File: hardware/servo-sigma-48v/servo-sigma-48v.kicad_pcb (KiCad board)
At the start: 4 copper layers, 71.7 x 73.2 mm, 198 parts, among them J1 CONN_01X02, J10 Conn_01x03, J11 Conn_01x03, J2 CONN_02X05, J3 CONN_01X03, J4 Conn_01x03, J5 Conn_01x05, J6 629_105_150_921, J7 CONN_01X02, J8 Conn_01x03, J9 Conn_01x03, Q1 STL160NS3LLH7, Q2 STL160NS3LLH7, Q3 STL160NS3LLH7, Q4 STL160NS3LLH7, Q5 STL160NS3LLH7, Q6 STL160NS3LLH7, Q7 STL160NS3LLH7, Q8 STL160NS3LLH7, SW1 SW_DIP_x08, SW2 SW_DIP_x08, U1 ST1S14, U10 OPA4374, U11 L6398, U12 SN65HVD75DGKR, U2 TPS70950, U3 SN65HVD75DGKR, U4 L6398, U5 STM32F411RETx, U6 L6398, U7 L6398, U8 TPS70933, U9 OPA4374, Y1 ABM3-8.000MHZ-D2Y-T

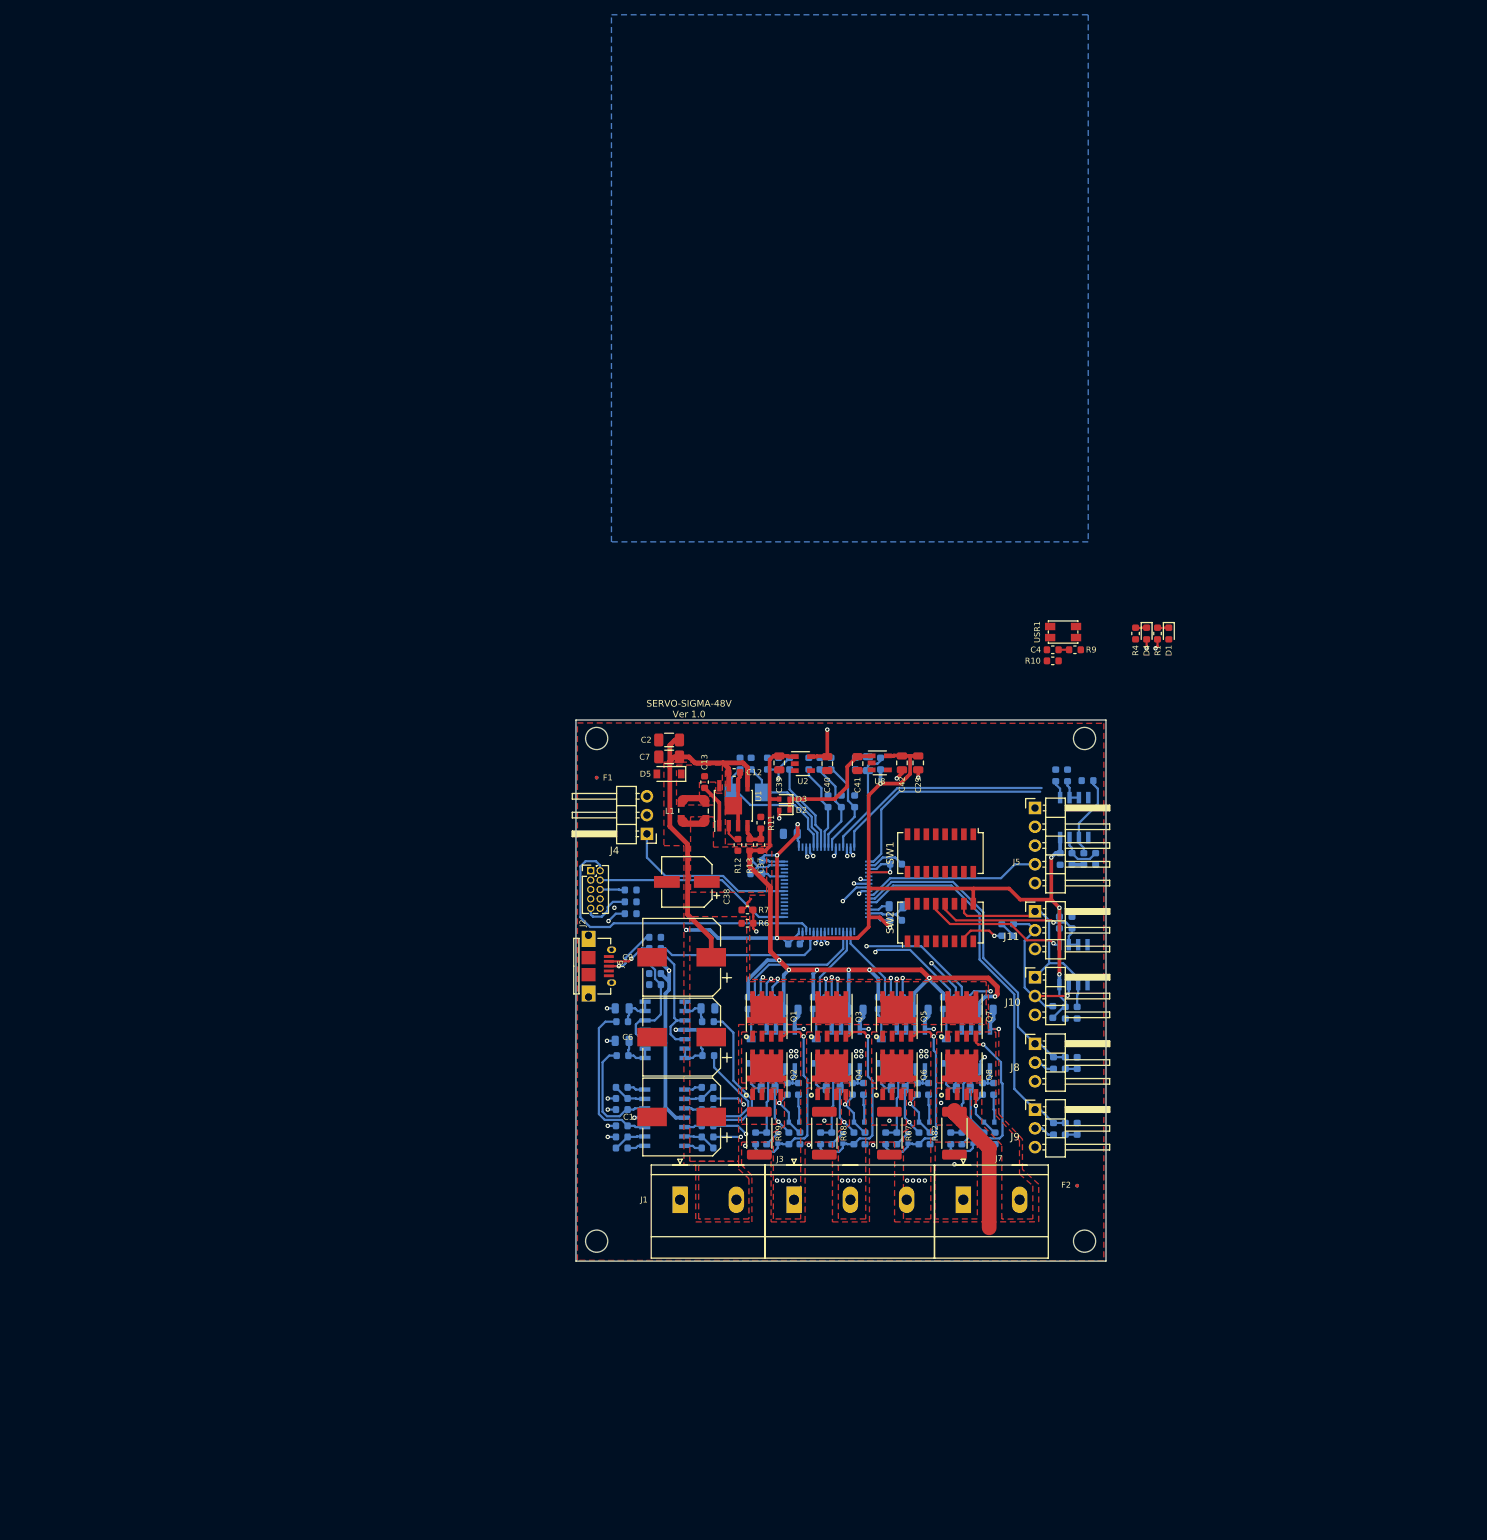
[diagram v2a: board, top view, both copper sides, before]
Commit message: Changed the MCU to use 100 pin
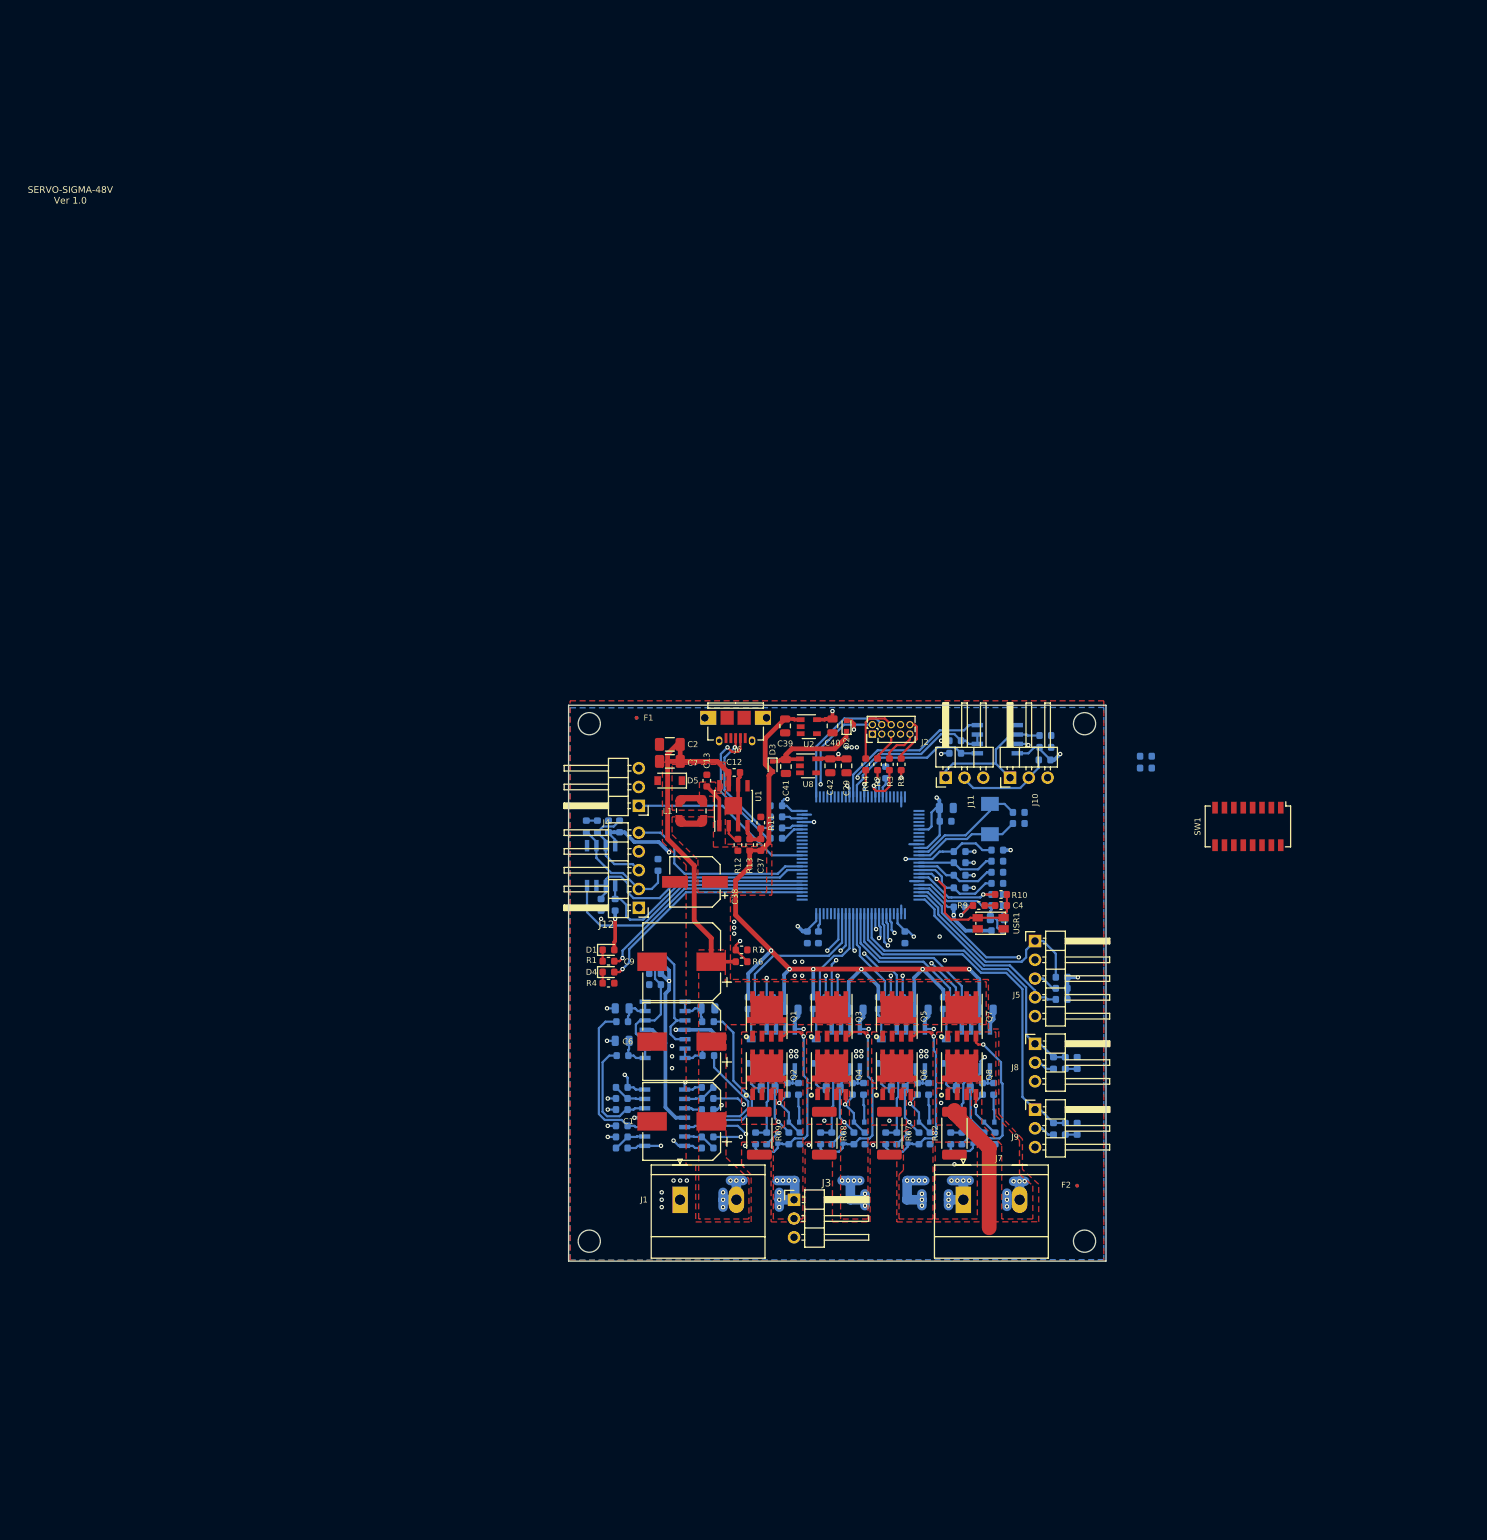
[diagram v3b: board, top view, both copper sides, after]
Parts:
- removed SW2: SW_DIP_x08, Button_Switch_SMD:SW_DIP_SPSTx08_Slide_Copal_CHS-08A_W5.08mm_P1.27mm_JPin
- added C10: 2.2uF, Capacitor_SMD:C_0603_1608Metric, B.Cu at (110.3, 77.3)
- added C53: 100nF 50V, Capacitor_SMD:C_0603_1608Metric, B.Cu at (129.4, 73.2)
- added C54: 100nF 50V, Capacitor_SMD:C_0603_1608Metric, B.Cu at (127.5, 61.6)
- added J12: Conn_01x05, Connector_PinHeader_2.54mm:PinHeader_1x05_P2.54mm_Horizontal, F.Cu at (86.0, 73.3)
- added R90: 10k, Resistor_SMD:R_0603_1608Metric, B.Cu at (143.2, 85.7)
- added R91: 10k, Resistor_SMD:R_0603_1608Metric, B.Cu at (143.2, 84.2)
- added R92: 10k, Resistor_SMD:R_0603_1608Metric, B.Cu at (143.2, 82.7)
- C15: value 4.7uF 25V -> 2.2uF; footprint Capacitor_SMD:C_0805_2012Metric -> Capacitor_SMD:C_0603_1608Metric
- J3: value CONN_01X03 -> Conn_01x03; footprint Sigmadrone:PhoenixContact_MKDS_03x7.62mm_Vertical -> Connector_PinHeader_2.54mm:PinHeader_1x03_P2.54mm_Horizontal
- R2, R3, R44, R5: moved to F.Cu
- U5: value STM32F411RETx -> STM32F405VGTx; footprint Package_QFP:LQFP-64_10x10mm_P0.5mm -> Package_QFP:LQFP-100_14x14mm_P0.5mm
- moved D1 87.0 mm to (81.9, 79.0), turned to 0 degrees
- moved R1 86.5 mm to (81.9, 80.5), turned to 180 degrees
- moved D4 86.0 mm to (81.9, 82.0), turned to 0 degrees
- moved R4 85.6 mm to (81.9, 83.5), turned to 180 degrees
- moved R83 67.4 mm to (78.9, 62.3), turned to 270 degrees
- moved R15 65.5 mm to (80.9, 72.9), turned to 270 degrees
- moved R38 64.6 mm to (83.4, 62.3)
- moved R81 64.4 mm to (80.4, 62.3), turned to 90 degrees
- moved U3 64.3 mm to (80.9, 67.6), turned to 90 degrees
- moved R14 62.1 mm to (82.8, 72.9), turned to 90 degrees
- moved C5 61.3 mm to (81.9, 62.3), turned to 270 degrees
- moved R40 59.2 mm to (88.6, 67.5), turned to 270 degrees
- moved J2 42.3 mm to (117.6, 49.8), turned to 90 degrees
- moved SW1 41.8 mm to (168.4, 62.3)
- moved USR1 40.6 mm to (133.6, 75.4), turned to 180 degrees
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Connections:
- C3 pad 2: /MCU/NRST -> Net-(C3-Pad2)
- C4 pad 2: /MCU/PB12 -> /MCU/PC3
- C51 pad 2: /MCU/PB1 -> /MCU/PB0
- C52 pad 2: /MCU/PB2 -> /MCU/PB1
- J5 pad 1: /MCU/ENCODER_B_CON -> /MCU/ENCODER_B
- J5 pad 3: /MCU/ENCODER_A_CON -> /MCU/ENCODER_A
- J5 pad 4: /MCU/ENCODER_Z_CON -> /MCU/ENCODER_Z
- J8 pad 1: /MCU/PB1 -> /MCU/PB0
- J9 pad 1: /MCU/PB2 -> /MCU/PB1
- Q1 pad 3: +BATT -> VIN
- Q3 pad 3: +BATT -> VIN
- Q5 pad 3: +BATT -> VIN
- Q7 pad 3: +BATT -> VIN
- R10 pad 2: /MCU/PB12 -> /MCU/PC3
- R17 pad 2: /MCU/PB1 -> /MCU/PB0
- R2 pad 1: /MCU/USART_RX -> /MCU/PB7
- R28 pad 2: /MCU/PB2 -> /MCU/PB1
- R3 pad 1: /MCU/USART_TX -> /MCU/PB6
- R38 pad 1: /MCU/ENCODER_RS485_B -> Net-(J12-Pad3)
- R40 pad 2: /MCU/ENCODER_RS485_A -> Net-(J12-Pad2)
- R45 pad 1: /MCU/SENSE_A -> /MCU/SENSE_C
- R45 pad 2: /MOSFETs/PHASE_A -> /MOSFETs/PHASE_C
- R46 pad 2: /MCU/SENSE_A -> /MCU/SENSE_C
- R5 pad 1: Net-(R5-Pad1) -> Net-(C3-Pad2)
- R50 pad 2: /MCU/USB_DP -> /MCU/PA12
- R51 pad 1: /MCU/SENSE_C -> /MCU/SENSE_A
- R51 pad 2: /MOSFETs/PHASE_C -> /MOSFETs/PHASE_A
- R52 pad 2: /MCU/SENSE_C -> /MCU/SENSE_A
- R6 pad 1: +BATT -> VIN
- R8 pad 1: /MCU/NRST -> Net-(C3-Pad2)
- R81 pad 1: /MCU/ENCODER_RS485_B -> Net-(J12-Pad3)
- R83 pad 2: /MCU/ENCODER_RS485_A -> Net-(J12-Pad2)
- R84 pad 2: /MCU/RS485_RO -> /MCU/PD6
- R85 pad 1: /MCU/RS485_DE -> /MCU/PD4
- SW1 pad 1: /MCU/ENCODER_DE -> Net-(SW1-Pad1)
- SW1 pad 12: /MCU/ENCODER_RS485_A -> Net-(SW1-Pad12)
- SW1 pad 13: /MCU/ENCODER_A -> Net-(SW1-Pad13)
- SW1 pad 14: /MCU/ENCODER_RS485_B -> Net-(SW1-Pad14)
- SW1 pad 15: /MCU/ENCODER_B_DE -> Net-(SW1-Pad15)
- SW1 pad 16: /MCU/ENCODER_B_DE -> Net-(SW1-Pad16)
- SW1 pad 2: /MCU/ENCODER_B_CON -> Net-(SW1-Pad2)
- SW1 pad 3: /MCU/ENCODER_B_CON -> Net-(SW1-Pad3)
- SW1 pad 4: /MCU/ENCODER_A_CON -> Net-(SW1-Pad4)
- SW1 pad 5: /MCU/ENCODER_A_CON -> Net-(SW1-Pad5)
- U12 pad 1: /MCU/RS485_RO -> /MCU/PD6
- U12 pad 2: /MCU/RS485_DE -> /MCU/PD4
- U12 pad 3: /MCU/RS485_DE -> /MCU/PD4
- U12 pad 4: /MCU/RS485_DI -> /MCU/PD5
- U3 pad 6: /MCU/ENCODER_RS485_A -> Net-(J12-Pad2)
- U3 pad 7: /MCU/ENCODER_RS485_B -> Net-(J12-Pad3)
- U5 pad 1: +3V3 -> /MCU/PE2
- U5 pad 10: /MCU/SENSE_C -> GND
- U5 pad 11: /MCU/IA_FB -> +3V3
- U5 pad 12: GND -> Net-(C27-Pad1)
- U5 pad 13: Net-(C30-Pad1) -> Net-(C32-Pad1)
- U5 pad 14: /MCU/ENCODER_A -> Net-(C3-Pad2)
- U5 pad 15: /MCU/ENCODER_B_DE -> /MCU/SENSE_C
- U5 pad 16: /MCU/ENCODER_DI -> /MCU/SENSE_B
- U5 pad 17: /MCU/ENCODER_RO -> /MCU/SENSE_A
- U5 pad 18: GND -> /MCU/PC3
- U5 pad 2: /MCU/PC13 -> /MCU/PE3
- U5 pad 20: /MCU/PA4 -> GND
- U5 pad 21: /MCU/PA5 -> Net-(C30-Pad1)
- U5 pad 22: /MCU/IR_FB -> +3V3
- U5 pad 23: /MCU/VBAT_ADC -> /MCU/ENCODER_A
- U5 pad 24: /MCU/IB_FB -> /MCU/ENCODER_B
- U5 pad 25: /MCU/IC_FB -> /MCU/ENCODER_Z
- U5 pad 26: /MCU/ENCODER_Z_CON -> /MCU/PA3
- U5 pad 27: /MCU/PB1 -> GND
- U5 pad 28: /MCU/PB2 -> +3V3
- U5 pad 29: /MCU/LED_STATUS -> /MCU/PA4
- U5 pad 3: /MCU/AUX_H -> /MCU/PE4
- U5 pad 30: Net-(C15-Pad2) -> /MCU/IA_FB
- U5 pad 31: GND -> /MCU/IB_FB
- U5 pad 32: +3V3 -> /MCU/IC_FB
- U5 pad 33: /MCU/PB12 -> /MCU/IR_FB
- U5 pad 34: /MCU/PWM_AL -> /MCU/VBAT_ADC
- U5 pad 35: /MCU/PWM_BL -> /MCU/PB0
- U5 pad 36: /MCU/PWM_CL -> /MCU/PB1
- U5 pad 37: /MCU/PC6 -> /MCU/AUX_H
- U5 pad 38: /MCU/PC7 -> /MCU/AUX_L
- U5 pad 39: /MCU/PC8 -> /MCU/PWM_AL
- U5 pad 4: /MCU/AUX_L -> /MCU/PE5
- U5 pad 40: /MCU/PC9 -> /MCU/PWM_AH
- U5 pad 41: /MCU/PWM_AH -> /MCU/PWM_BL
- U5 pad 43: /MCU/PWM_CH -> /MCU/PWM_CL
- U5 pad 44: /MCU/PA11 -> /MCU/PWM_CH
- U5 pad 45: /MCU/PA12 -> /MCU/PE14
- U5 pad 46: /MCU/PA13 -> /MCU/PE15
- U5 pad 47: GND -> /MCU/PB10
- U5 pad 48: +3V3 -> /MCU/PB11
- U5 pad 49: /MCU/PA14 -> Net-(C10-Pad2)
- U5 pad 5: Net-(C27-Pad1) -> /MCU/PE6
- U5 pad 50: /MCU/PA15 -> +3V3
- U5 pad 51: /MCU/PC10 -> /MCU/PB12
- U5 pad 52: /MCU/PC11 -> /MCU/PB13
- U5 pad 53: /MCU/PC12 -> /MCU/LED_WARN
- U5 pad 54: /MCU/PD2 -> /MCU/LED_STATUS
- U5 pad 55: /MCU/PB3 -> /MCU/ENCODER_DI
- U5 pad 56: /MCU/PWM -> /MCU/ENCODER_RO
- U5 pad 57: /MCU/PB5 -> /MCU/PD10
- U5 pad 58: /MCU/PB6 -> /MCU/PD11
- U5 pad 59: /MCU/PB7 -> /MCU/ENCODER_DE
- U5 pad 6: Net-(C32-Pad1) -> +3V3
- U5 pad 60: /MCU/BOOT0 -> /MCU/ENCODER_RS485_MCLR
- U5 pad 61: /MCU/PB8 -> /MCU/PD14
- U5 pad 62: /MCU/LED_WARN -> /MCU/PD15
- U5 pad 63: GND -> /MCU/PWM
- U5 pad 64: +3V3 -> /MCU/PC7
- U5 pad 7: Net-(R5-Pad1) -> /MCU/PC13
- U5 pad 8: /MCU/SENSE_A -> /MCU/PC14
- U5 pad 9: /MCU/SENSE_B -> /MCU/PC15
- USR1 pad 2: /MCU/PB12 -> /MCU/PC3
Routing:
- net +3V3: track 216.2 -> 326.5 mm, vias 11 -> 14
- net /MOSFETs/PHASE_C: track 9.99 -> 64.6 mm, vias 9 -> 13
- net /MCU/PB2: track 52.0 -> 0.00 mm
- net /MOSFETs/PHASE_B: track 10.0 -> 53.2 mm, vias 9 -> 13
- net /MCU/PB0: track 0.00 -> 39.9 mm
- net /MCU/NRST: track 41.9 -> 6.21 mm, vias 1 -> 0
- net /MOSFETs/PHASE_A: track 9.99 -> 44.8 mm, vias 9 -> 13
- net /MCU/ENCODER_DE: track 3.59 -> 34.4 mm
- net /MCU/LED_WARN: track 1.20 -> 30.9 mm
- net /MCU/LED_STATUS: track 1.36 -> 30.1 mm
- net /MCU/ENCODER_B: track 0.00 -> 28.4 mm
- net /MCU/ENCODER_RS485_MCLR: track 0.00 -> 26.2 mm
- net /MCU/EXT_5V: track 37.2 -> 11.1 mm, vias 2 -> 1
- net Net-(C3-Pad2): track 0.00 -> 25.1 mm, vias 0 -> 2
- net /MCU/ENCODER_Z: track 0.00 -> 24.5 mm
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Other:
- board size 71.7 x 73.2 mm -> 72.7 x 75.2 mm

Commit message: Routed version 2.0
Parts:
- added C55: 100nF 50V, Capacitor_SMD:C_0603_1608Metric, B.Cu at (123.3, 55.0)
- J3: value Conn_01x03 -> CONN_01X03; footprint Connector_PinHeader_2.54mm:PinHeader_1x03_P2.54mm_Horizontal -> Sigmadrone:PhoenixContact_MKDS_03x7.62mm_Vertical
- R88, R89: moved to F.Cu
- SW1: value SW_DIP_x08 -> SW_DIP_x04; footprint Button_Switch_SMD:SW_DIP_SPSTx08_Slide_Copal_CHS-08A_W5.08mm_P1.27mm_JPin -> Button_Switch_SMD:SW_DIP_SPSTx04_Slide_Copal_CHS-04A_W5.08mm_P1.27mm_JPin
- moved SW1 47.1 mm to (121.3, 60.8), turned to 180 degrees
- moved R88 25.7 mm to (129.5, 58.2)
- moved R89 25.7 mm to (129.5, 59.7), turned to 180 degrees
- moved C29 0.20 mm to (113.9, 54.1)
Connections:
- SW1 pad 1: Net-(SW1-Pad1) -> +3V3
- SW1 pad 2: Net-(SW1-Pad2) -> +3V3
- SW1 pad 3: Net-(SW1-Pad3) -> /MCU/B_TERM_R120
- SW1 pad 4: Net-(SW1-Pad4) -> +3V3
- SW1 pad 5: Net-(SW1-Pad5) -> /MCU/BOOT0
- SW1 pad 6: Net-(SW1-Pad6) -> /MCU/A_TERM_R120
- SW1 pad 7: Net-(SW1-Pad7) -> /MCU/GPIO_CONF_2
- SW1 pad 8: Net-(SW1-Pad8) -> /MCU/GPIO_CONF_1
- U5 pad 97: /MCU/PE0 -> /MCU/GPIO_CONF_2
- U5 pad 98: /MCU/PE1 -> /MCU/GPIO_CONF_1
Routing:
- net +3V3: track 326.5 -> 342.4 mm
- net /MCU/A_TERM_R120: track 19.5 -> 31.1 mm
- net +5V: track 165.7 -> 175.8 mm
- net VIN: track 56.5 -> 63.5 mm
- net /MCU/GPIO_CONF_1: track 0.00 -> 5.82 mm, vias 0 -> 1
- net /MCU/B_TERM_R120: track 0.00 -> 5.06 mm
- net /MCU/GPIO_CONF_2: track 0.00 -> 4.39 mm, vias 0 -> 1
- net GND: track 214.9 -> 219.1 mm, vias 46 -> 50
- net Net-(J10-Pad2): track 19.4 -> 22.5 mm
- net +15V: track 121.4 -> 124.1 mm
- net /MCU/BOOT0: track 2.68 -> 5.04 mm, vias 0 -> 1
- net /MCU/PB6: track 6.67 -> 4.98 mm
- net Net-(R88-Pad2): track 0.00 -> 1.51 mm
